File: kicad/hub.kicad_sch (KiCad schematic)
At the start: 45 parts, among them J201 Conn_01x05_Pin, U201 USB5807, Y201 25Mhz 50ppm

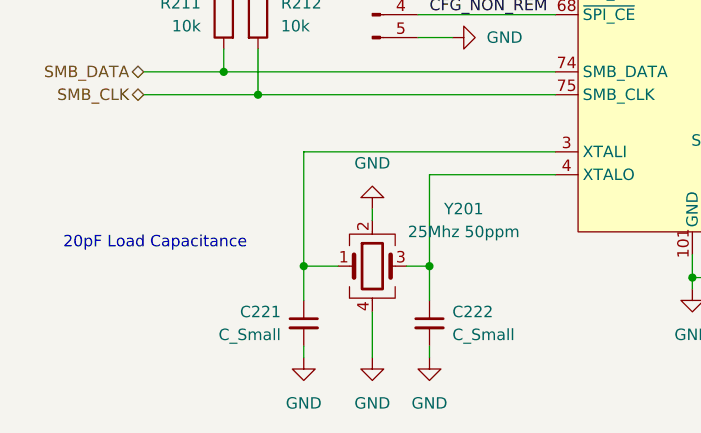
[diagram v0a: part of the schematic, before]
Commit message: First rough placement
Just to get an idea on how it might look like
Added trace widts for Differential pairs
Using 6 layers, because it makes power management easier.
Rather large PCB, but better to big, then to small.
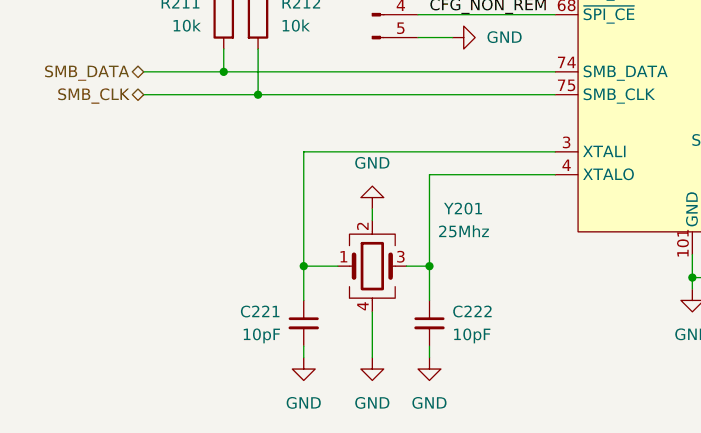
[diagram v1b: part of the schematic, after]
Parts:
- C221, C222: value C_Small -> 10pF
- Y201: value 25Mhz 50ppm -> 25Mhz; footprint (none) -> Crystal:Crystal_SMD_Abracon_ABM8G-4Pin_3.2x2.5mm; PartNo (none) -> ABM8G-25.000MHZ-B4Y-T
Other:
- note removed: "20pF Load Capacitance"
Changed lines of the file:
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@@
 		)
 	)
-	(text "20pF Load Capacitance"
-		(exclude_from_sim no)
-		(at 29.21 179.07 0)
-		(effects
-			(font
-				(size 1.27 1.27)
-			)
-		)
-	)
 	(text "USB 3.0 HUB"
 		(exclude_from_sim no)
@@
 	(label "Port6.SSTX-"
 		(at 203.2 82.55 0)
+		(fields_autoplaced yes)
 		(effects
 			(font
@@
 	(label "Port6.SSRX-"
 		(at 203.2 90.17 0)
+		(fields_autoplaced yes)
 		(effects
 			(font
@@
 	(label "Port6.SSTX+"
 		(at 203.2 85.09 0)
+		(fields_autoplaced yes)
 		(effects
 			(font
@@
 	(label "Port6.SPEED_IND"
 		(at 203.2 100.33 0)
+		(fields_autoplaced yes)
 		(effects
 			(font
@@
 	(label "Port6.DP+"
 		(at 203.2 77.47 0)
+		(fields_autoplaced yes)
 		(effects
 			(font
@@
 	(label "Port6.PRT_CTRL"
 		(at 203.2 97.79 0)
+		(fields_autoplaced yes)
 		(effects
 			(font
@@
 	(label "Port6.SSRX+"
 		(at 203.2 92.71 0)
+		(fields_autoplaced yes)
 		(effects
 			(font
@@
 	(label "Port6.DP-"
 		(at 203.2 74.93 0)
+		(fields_autoplaced yes)
 		(effects
 			(font
@@
 			)
 		)
-		(property "Value" "25Mhz 50ppm"
+		(property "Value" "25Mhz"
 			(at 63.5 177.8 0)
 			(effects
@@
 			)
 		)
-		(property "Footprint" ""
+		(property "Footprint" "Crystal:Crystal_SMD_Abracon_ABM8G-4Pin_3.2x2.5mm"
 			(at 53.34 181.61 0)
 			(effects
@@
 			)
 		)
+		(property "PartNo" "ABM8G-25.000MHZ-B4Y-T"
+			(at 53.34 181.61 0)
+			(effects
+				(font
+					(size 1.27 1.27)
+				)
+				(hide yes)
+			)
+		)
 		(pin "2"
 		)
@@
 			)
 		)
-		(property "Value" "C_Small"
+		(property "Value" "10pF"
 			(at 43.18 189.2362 0)
 			(effects
@@
 			)
 		)
-		(property "Value" "C_Small"
+		(property "Value" "10pF"
 			(at 62.23 189.2362 0)
 			(effects

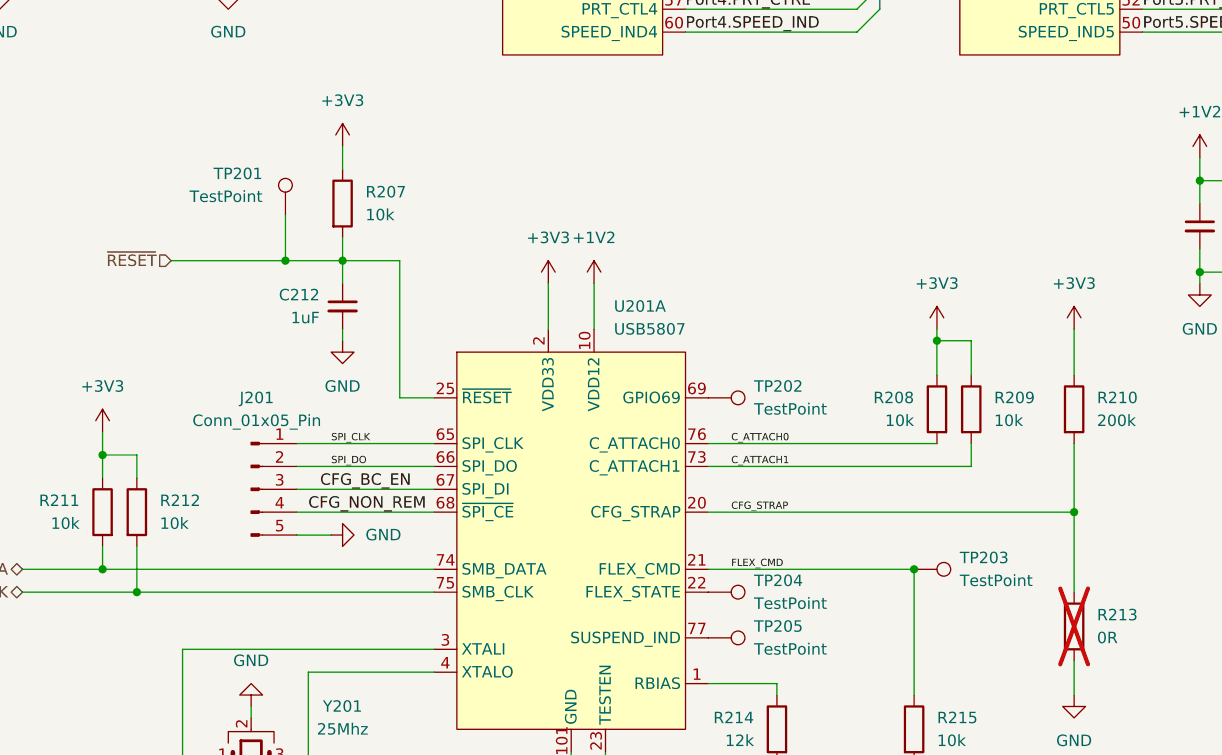
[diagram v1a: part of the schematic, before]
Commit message: Added first fanout for usb5807
Needs a lot more work, but it is a start, that allows me to concentrate
on the routing of USB signals and have the capacitors relatively close
to the hub controller.
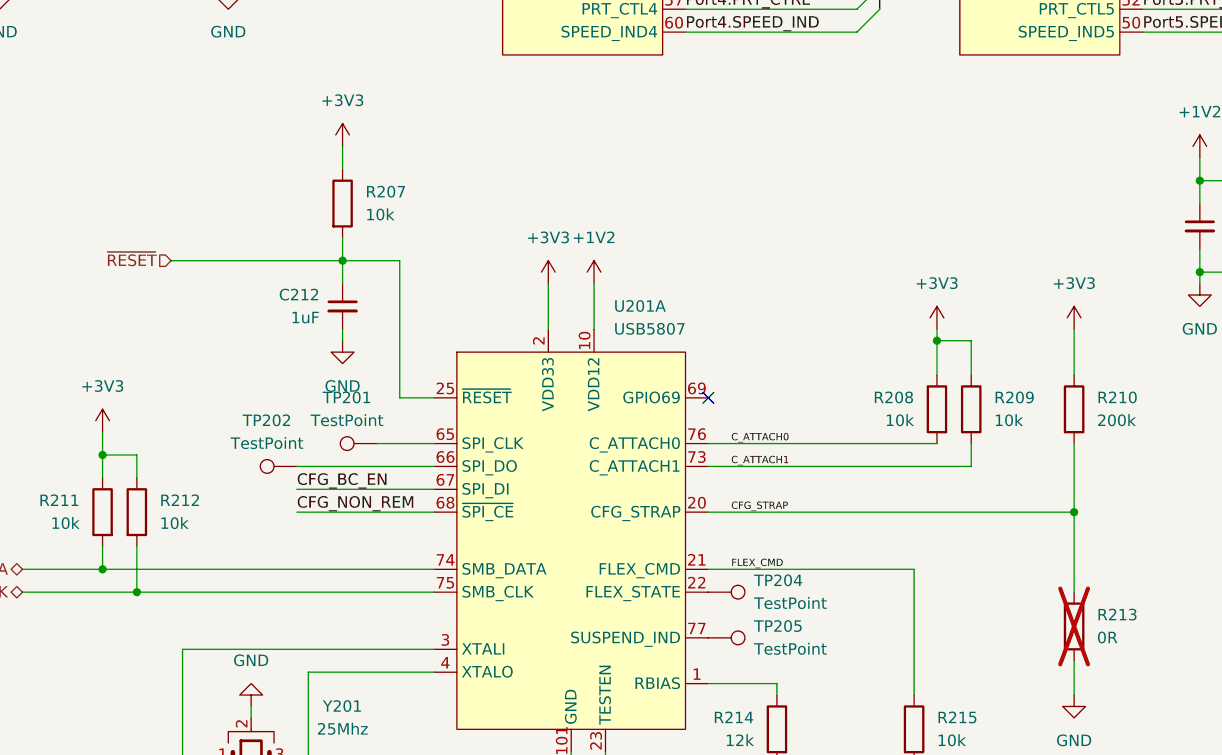
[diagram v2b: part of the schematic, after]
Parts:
- removed J201: Conn_01x05_Pin, Connector_PinHeader_2.54mm:PinHeader_1x05_P2.54mm_Vertical, symbol Connector:Conn_01x05_Pin
- removed TP203: TestPoint, Connector_PinHeader_2.54mm:PinHeader_1x01_P2.54mm_Vertical, symbol Connector:TestPoint
- TP201, TP202, TP204, TP205: footprint Connector_PinHeader_2.54mm:PinHeader_1x01_P2.54mm_Vertical -> TestPoint:TestPoint_Pad_D1.0mm
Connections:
- net SPI_DO is gone; now on an unnamed net: U201.66 (SPI_DO)
- net ~{RESET}: no longer TP201.1
- net at TP202.1: no longer U201.69 (GPIO69)
- net SPI_CLK: no longer names the net of U201.65 (SPI_CLK)
- net SPI_CLK: now also TP201.1
- no-connect marks 5 -> 6
